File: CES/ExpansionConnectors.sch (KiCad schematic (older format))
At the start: 4 parts

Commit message: Control Unit
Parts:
- gave numbers to parts that had none: 4
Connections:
- net A14: no longer names the net of J1701.15 (Pin_15)
- net A15: no longer names the net of J1701.16 (Pin_16)
- no-connect marks 0 -> 2
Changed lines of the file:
@@
 $Descr A4 11693 8268
 encoding utf-8
-Sheet 16 16
+Sheet 17 17
 Title ""
 Date ""
@@
 $EndDescr
 $Comp
-L Connector:Conn_01x16_Female J?
+L Connector:Conn_01x16_Female J1701
 U 1 1 60990C84
 P 3200 1700
-F 0 "J?" H 3250 800 50  0000 R CNN
+F 0 "J1701" H 3250 800 50  0000 R CNN
 F 1 "AddressBusConnector" H 3600 2600 50  0000 R CNN
 F 2 "" H 3200 1700 50  0001 C CNN
@@
 $EndComp
 $Comp
-L Connector:Conn_01x16_Female J?
+L Connector:Conn_01x16_Female J1702
 U 1 1 60994D8B
 P 3200 3900
-F 0 "J?" H 3250 3000 50  0000 R CNN
+F 0 "J1702" H 3250 3000 50  0000 R CNN
 F 1 "DataBusConnector" H 3600 4800 50  0000 R CNN
 F 2 "" H 3200 3900 50  0001 C CNN
@@
 $EndComp
 $Comp
-L Connector:Conn_01x16_Female J?
+L Connector:Conn_01x16_Female J1703
 U 1 1 609975FA
 P 3200 6050
-F 0 "J?" H 3200 5150 50  0000 R CNN
+F 0 "J1703" H 3200 5150 50  0000 R CNN
 F 1 "RTConnector" H 3600 6950 50  0000 R CNN
 F 2 "" H 3200 6050 50  0001 C CNN
@@
 Wire Wire Line
 	2000 2300 3000 2300
-Text GLabel 2000 2400 0    50   Input ~ 0
-A14
-Wire Wire Line
-	2000 2400 3000 2400
-Text GLabel 2000 2500 0    50   Input ~ 0
-A15
-Wire Wire Line
-	2000 2500 3000 2500
 Text GLabel 6500 1400 0    50   Input ~ 0
 ~SelRam
@@
 ~HabSaiRAM
 $Comp
-L power:VCC #PWR?
+L power:VCC #PWR01701
 U 1 1 609B015B
 P 7250 900
-F 0 "#PWR?" H 7250 750 50  0001 C CNN
+F 0 "#PWR01701" H 7250 750 50  0001 C CNN
 F 1 "VCC" H 7265 1073 50  0000 C CNN
 F 2 "" H 7250 900 50  0001 C CNN
@@
 $EndComp
 $Comp
-L power:GND #PWR?
+L power:GND #PWR01702
 U 1 1 609B027B
 P 7250 1250
-F 0 "#PWR?" H 7250 1000 50  0001 C CNN
+F 0 "#PWR01702" H 7250 1000 50  0001 C CNN
 F 1 "GND" H 7100 1150 50  0000 C CNN
 F 2 "" H 7250 1250 50  0001 C CNN
@@
 $EndComp
 $Comp
-L Connector:Conn_01x07_Female J?
+L Connector:Conn_01x07_Female J1704
 U 1 1 609B0E5F
 P 7700 1300
-F 0 "J?" H 7650 900 50  0000 L CNN
+F 0 "J1704" H 7650 900 50  0000 L CNN
 F 1 "MemSignalsConnector" H 7300 1750 50  0000 L CNN
 F 2 "" H 7700 1300 50  0001 C CNN
@@
 	7250 1000 7250 900
 Connection ~ 7400 1000
+NoConn ~ 3000 2400
+NoConn ~ 3000 2500
 $EndSCHEMATC

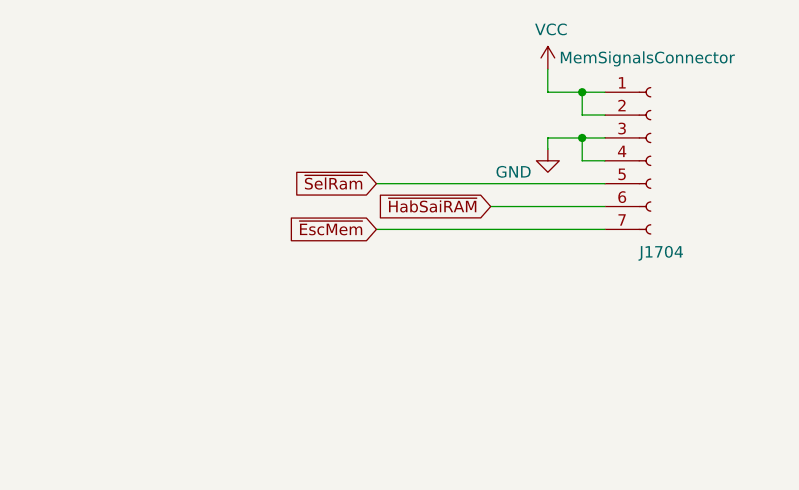
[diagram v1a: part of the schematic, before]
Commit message: Correcting ERC issues
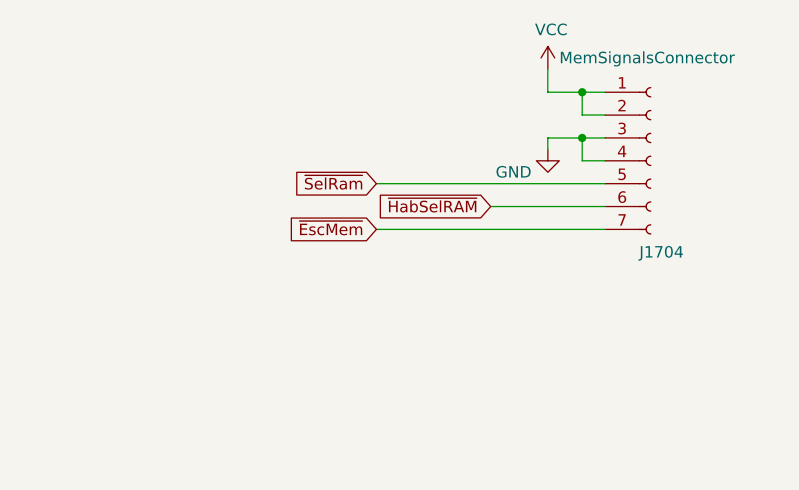
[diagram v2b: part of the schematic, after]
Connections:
- net ~HabSaiRAM renamed ~HabSelRAM
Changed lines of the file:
@@
 $Descr A4 11693 8268
 encoding utf-8
-Sheet 17 17
+Sheet 17 18
 Title ""
 Date ""
@@
 ~EscMem
 Text GLabel 7000 1500 0    50   Input ~ 0
-~HabSaiRAM
+~HabSelRAM
 $Comp
 L power:VCC #PWR01701

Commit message: Assigning footprints and generating netlist
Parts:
- J1701, J1702, J1703: footprint (none) -> Connector_PinHeader_2.54mm:PinHeader_1x16_P2.54mm_Vertical
- J1704: footprint (none) -> Connector_PinHeader_2.54mm:PinHeader_1x07_P2.54mm_Vertical
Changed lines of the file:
@@
 F 0 "J1701" H 3250 800 50  0000 R CNN
 F 1 "AddressBusConnector" H 3600 2600 50  0000 R CNN
-F 2 "" H 3200 1700 50  0001 C CNN
+F 2 "Connector_PinHeader_2.54mm:PinHeader_1x16_P2.54mm_Vertical" H 3200 1700 50  0001 C CNN
 F 3 "~" H 3200 1700 50  0001 C CNN
 	1    3200 1700
@@
 F 0 "J1702" H 3250 3000 50  0000 R CNN
 F 1 "DataBusConnector" H 3600 4800 50  0000 R CNN
-F 2 "" H 3200 3900 50  0001 C CNN
+F 2 "Connector_PinHeader_2.54mm:PinHeader_1x16_P2.54mm_Vertical" H 3200 3900 50  0001 C CNN
 F 3 "~" H 3200 3900 50  0001 C CNN
 	1    3200 3900
@@
 F 0 "J1703" H 3200 5150 50  0000 R CNN
 F 1 "RTConnector" H 3600 6950 50  0000 R CNN
-F 2 "" H 3200 6050 50  0001 C CNN
+F 2 "Connector_PinHeader_2.54mm:PinHeader_1x16_P2.54mm_Vertical" H 3200 6050 50  0001 C CNN
 F 3 "~" H 3200 6050 50  0001 C CNN
 	1    3200 6050
@@
 F 0 "J1704" H 7650 900 50  0000 L CNN
 F 1 "MemSignalsConnector" H 7300 1750 50  0000 L CNN
-F 2 "" H 7700 1300 50  0001 C CNN
+F 2 "Connector_PinHeader_2.54mm:PinHeader_1x07_P2.54mm_Vertical" H 7700 1300 50  0001 C CNN
 F 3 "~" H 7700 1300 50  0001 C CNN
 	1    7700 1300

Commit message: Correcting footprints errors
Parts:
- J1701: value AddressBusConnector -> Conn_01x16
- J1702: value DataBusConnector -> Conn_01x16
- J1703: value RTConnector -> Conn_01x16
- J1704: value MemSignalsConnector -> Conn_01x07
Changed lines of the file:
@@
 P 3200 1700
 F 0 "J1701" H 3250 800 50  0000 R CNN
-F 1 "AddressBusConnector" H 3600 2600 50  0000 R CNN
+F 1 "Conn_01x16" H 3600 2600 50  0000 R CNN
 F 2 "Connector_PinHeader_2.54mm:PinHeader_1x16_P2.54mm_Vertical" H 3200 1700 50  0001 C CNN
 F 3 "~" H 3200 1700 50  0001 C CNN
@@
 P 3200 3900
 F 0 "J1702" H 3250 3000 50  0000 R CNN
-F 1 "DataBusConnector" H 3600 4800 50  0000 R CNN
+F 1 "Conn_01x16" H 3600 4800 50  0000 R CNN
 F 2 "Connector_PinHeader_2.54mm:PinHeader_1x16_P2.54mm_Vertical" H 3200 3900 50  0001 C CNN
 F 3 "~" H 3200 3900 50  0001 C CNN
@@
 P 3200 6050
 F 0 "J1703" H 3200 5150 50  0000 R CNN
-F 1 "RTConnector" H 3600 6950 50  0000 R CNN
+F 1 "Conn_01x16" H 3600 6950 50  0000 R CNN
 F 2 "Connector_PinHeader_2.54mm:PinHeader_1x16_P2.54mm_Vertical" H 3200 6050 50  0001 C CNN
 F 3 "~" H 3200 6050 50  0001 C CNN
@@
 P 7700 1300
 F 0 "J1704" H 7650 900 50  0000 L CNN
-F 1 "MemSignalsConnector" H 7300 1750 50  0000 L CNN
+F 1 "Conn_01x07" H 7300 1750 50  0000 L CNN
 F 2 "Connector_PinHeader_2.54mm:PinHeader_1x07_P2.54mm_Vertical" H 7700 1300 50  0001 C CNN
 F 3 "~" H 7700 1300 50  0001 C CNN
